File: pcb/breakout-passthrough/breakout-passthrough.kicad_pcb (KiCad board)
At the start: 4 copper layers, 38.4 x 62 mm, 2 parts, among them J1 FX18-120P-0.8SV20, J2 FX18-120S-0.8SV20

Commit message: [pass] ab based labels
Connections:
- net /IOB_102 renamed /HG_08
- net /IOB_56 renamed /LK_08
- net /IOB_57 renamed /LK_07
- net /IOB_61 renamed /LK_06
- net /IOB_63 renamed /LK_05
- net /IOB_64 renamed /LK_04
- net /IOB_71 renamed /LK_03
- net /IOB_72 renamed /LK_02
- net /IOB_73 renamed /LK_01
- net /IOB_79 renamed /JI_08
- net /IOB_80 renamed /JI_07
- net /IOB_81 renamed /JI_06
- net /IOB_82 renamed /JI_05
- net /IOB_91 renamed /JI_04
- net /IOB_94 renamed /JI_03
- net /IOB_95 renamed /JI_02
- net /IOB_96 renamed /JI_01
- net /IOL_10A renamed /GH_08
- net /IOL_10B renamed /IJ_01
- net /IOL_12A renamed /IJ_02
- net /IOL_12B renamed /IJ_03
- net /IOL_13A renamed /IJ_04
- net /IOL_13B renamed /IJ_05
- net /IOL_14B renamed /IJ_06
- net /IOL_17A renamed /IJ_07
- net /IOL_17B renamed /IJ_08
- net /IOL_18A renamed /KL_01
- net /IOL_18B renamed /KL_02
- net /IOL_23A renamed /KL_03
- net /IOL_23B renamed /KL_04
- net /IOL_24A renamed /KL_05
- net /IOL_24B renamed /KL_06
- net /IOL_25A renamed /KL_07
- net /IOL_25B renamed /KL_08
- net /IOL_4A renamed /GH_02
- net /IOL_4B renamed /GH_03
- net /IOL_5A renamed /GH_04
- net /IOL_5B renamed /GH_05
- net /IOL_8A renamed /GH_06
- net /IOL_8B renamed /GH_07
- net /IOR_109 renamed /HG_07
- net /IOR_110 renamed /HG_06
- net /IOR_111 renamed /HG_05
- net /IOR_112 renamed /HG_04
- net /IOR_114 renamed /HG_03
- net /IOR_115 renamed /HG_02
- net /IOR_116 renamed /HG_01
- net /IOR_117 renamed /FE_08
- net /IOR_118 renamed /FE_07
- net /IOR_119 renamed /FE_06
- net /IOR_120 renamed /FE_05
- net /IOR_128 renamed /FE_04
- net /IOR_136 renamed /FE_03
- net /IOR_137 renamed /FE_02
- net /IOR_138 renamed /FE_01
- net /IOR_139 renamed /DC_08
- net /IOR_140 renamed /DC_07
- net /IOR_141 renamed /DC_06
- net /IOR_144 renamed /DC_05
- net /IOR_146 renamed /DC_04
- net /IOR_147 renamed /DC_03
- net /IOR_148 renamed /DC_02
- net /IOR_152 renamed /DC_01
- net /IOR_160 renamed /BA_08
- net /IOR_161 renamed /BA_07
- net /IOR_164 renamed /BA_06
- net /IOR_165 renamed /BA_05
- net /IOR_166 renamed /BA_04
- net /IOR_167 renamed /BA_03
- net /IOT_168 renamed /BA_02
- net /IOT_169 renamed /BA_01
- net /IOT_170 renamed /CD_08
- net /IOT_171 renamed /CD_07
- net /IOT_172 renamed /CD_06
- net /IOT_173 renamed /CD_05
- net /IOT_174 renamed /CD_04
- net /IOT_177 renamed /CD_03
- net /IOT_178 renamed /CD_02
- net /IOT_179 renamed /CD_01
- net /IOT_181 renamed /AB_08
- net /IOT_190 renamed /AB_07
- net /IOT_191 renamed /AB_06
- net /IOT_192 renamed /AB_05
- net /IOT_197 renamed /AB_04
- net /IOT_198 renamed /AB_03
- net /IOT_206 renamed /AB_02
- net /IOT_212 renamed /AB_01
- net /IOT_213 renamed /EF_01
- net /IOT_214 renamed /EF_02
- net /IOT_215 renamed /EF_03
- net /IOT_216 renamed /EF_04
- net /IOT_217 renamed /EF_05
- net /IOT_219 renamed /EF_06
- net /IOT_220 renamed /EF_07
- net /IOT_221 renamed /EF_08
- net /IOT_222 renamed /GH_01

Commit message: [pcb] prep work for FX18-120P footprint fix
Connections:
- net /+3V3 renamed +3V3
- net /AB_01 renamed /A_01
- net /AB_02 renamed /A_05
- net /AB_03 renamed /A_02
- net /AB_04 renamed /A_06
- net /AB_05 renamed /A_03
- net /AB_06 renamed /A_07
- net /AB_07 renamed /A_04
- net /AB_08 renamed /A_08
- net /BA_01 renamed /E_01
- net /BA_02 renamed /E_05
- net /BA_03 renamed /E_02
- net /BA_04 renamed /E_06
- net /BA_05 renamed /E_03
- net /BA_06 renamed /E_07
- net /BA_07 renamed /E_04
- net /BA_08 renamed /E_08
- net /CD_01 renamed /B_01
- net /CD_02 renamed /B_05
- net /CD_03 renamed /B_02
- net /CD_04 renamed /B_06
- net /CD_05 renamed /B_03
- net /CD_06 renamed /B_07
- net /CD_07 renamed /B_04
- net /CD_08 renamed /B_08
- net /DC_01 renamed /F_01
- net /DC_02 renamed /F_05
- net /DC_03 renamed /F_02
- net /DC_04 renamed /F_06
- net /DC_05 renamed /F_03
- net /DC_06 renamed /F_07
- net /DC_07 renamed /F_04
- net /DC_08 renamed /F_08
- net /EF_01 renamed /C_01
- net /EF_02 renamed /C_05
- net /EF_03 renamed /C_02
- net /EF_04 renamed /C_06
- net /EF_05 renamed /C_03
- net /EF_06 renamed /C_07
- net /EF_07 renamed /C_04
- net /EF_08 renamed /C_08
- net /FE_01 renamed /L_08
- net /FE_02 renamed /L_04
- net /FE_03 renamed /L_07
- net /FE_04 renamed /L_03
- net /FE_05 renamed /L_06
- net /FE_06 renamed /L_02
- net /FE_07 renamed /L_05
- net /FE_08 renamed /L_01
- net /GH_01 renamed /D_01
- net /GH_02 renamed /D_05
- net /GH_03 renamed /D_02
- net /GH_04 renamed /D_06
- net /GH_05 renamed /D_03
- net /GH_06 renamed /D_07
- net /GH_07 renamed /D_04
- net /GH_08 renamed /D_08
- net /HG_01 renamed /I_01
- net /HG_02 renamed /I_05
- net /HG_03 renamed /I_02
- net /HG_04 renamed /I_06
- net /HG_05 renamed /I_03
- net /HG_06 renamed /I_07
- net /HG_07 renamed /I_04
- net /HG_08 renamed /I_08
- net /IJ_01 renamed /G_01
- net /IJ_02 renamed /G_05
- net /IJ_03 renamed /G_02
- net /IJ_04 renamed /G_06
- net /IJ_05 renamed /G_03
- net /IJ_06 renamed /G_07
- net /IJ_07 renamed /G_04
- net /IJ_08 renamed /G_08
- net /JI_01 renamed /K_08
- net /JI_02 renamed /K_04
- net /JI_03 renamed /K_07
- net /JI_04 renamed /K_03
- net /JI_05 renamed /K_06
- net /JI_06 renamed /K_02
- net /JI_07 renamed /K_05
- net /JI_08 renamed /K_01
- net /KL_01 renamed /H_01
- net /KL_02 renamed /H_05
- net /KL_03 renamed /H_02
- net /KL_04 renamed /H_06
- net /KL_05 renamed /H_03
- net /KL_06 renamed /H_07
- net /KL_07 renamed /H_04
- net /KL_08 renamed /H_08
- net /LK_01 renamed /J_01
- net /LK_02 renamed /J_05
- net /LK_03 renamed /J_02
- net /LK_04 renamed /J_06
- net /LK_05 renamed /J_03
- net /LK_06 renamed /J_07
- net /LK_07 renamed /J_04
- net /LK_08 renamed /J_08

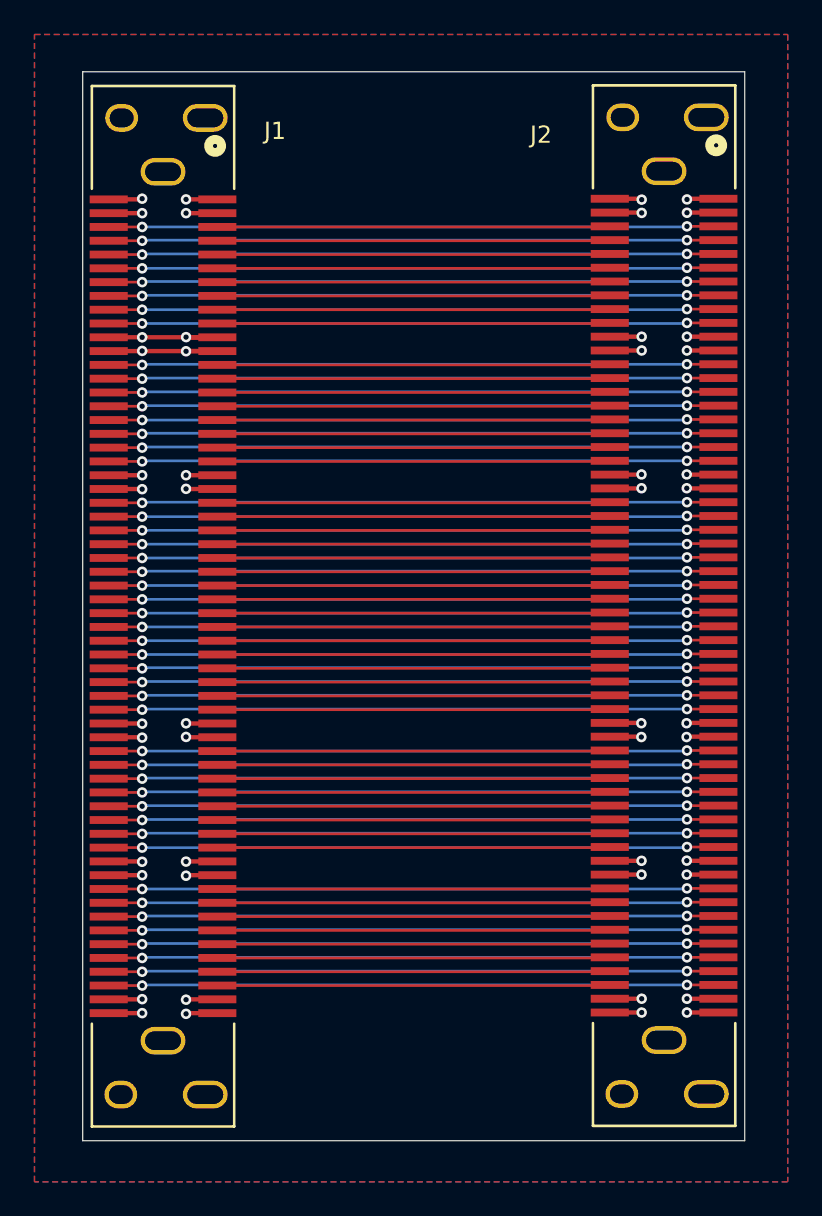
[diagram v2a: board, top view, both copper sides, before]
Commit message: [pcb] add FX18-120P footprint and update pcbs
and a few adc fixes, including a key resistor fix
(the op amp for Y had a copy paste error from X
on the positive Rg)
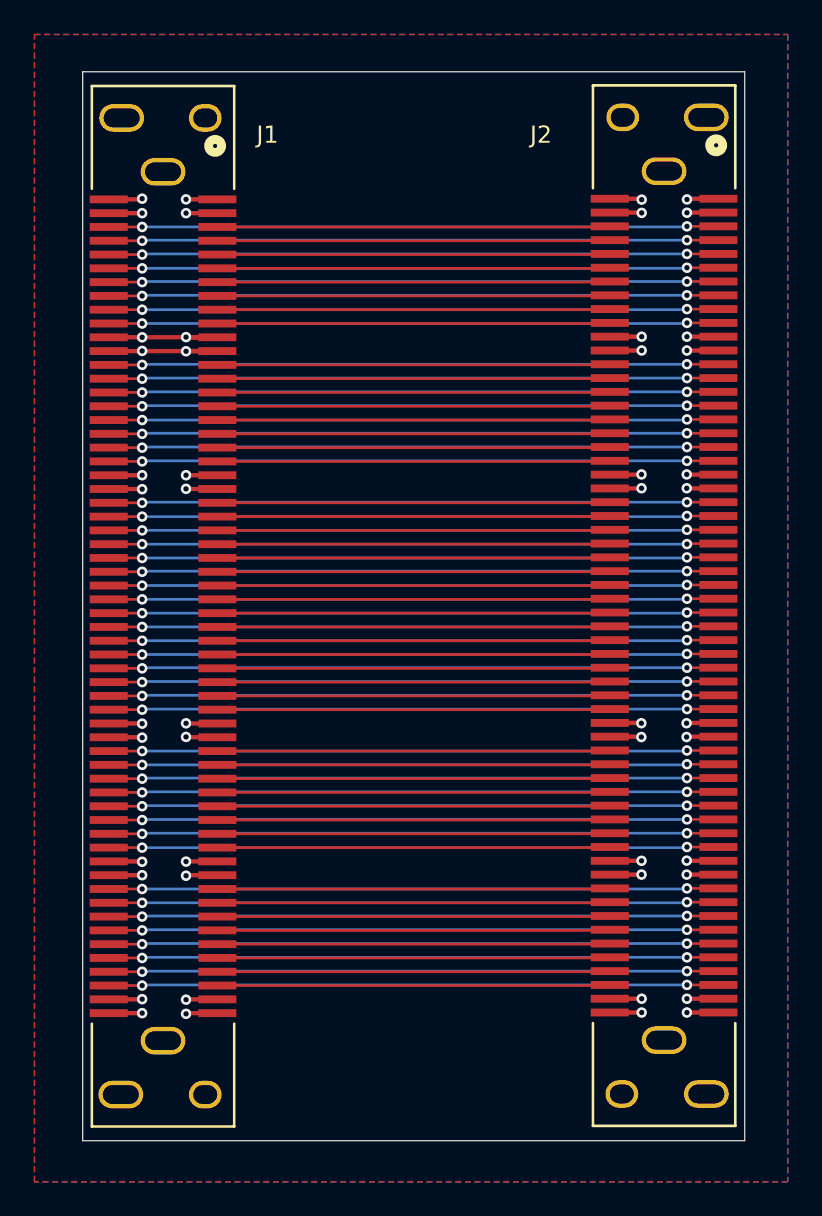
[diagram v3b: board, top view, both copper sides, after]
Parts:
- J1: footprint custom:CUSTOM_FX_120S-0.8SH20 -> custom:CUSTOM_FX_120P-0.8SH20
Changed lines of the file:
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@@
 		)
 	)
-	(footprint "custom:CUSTOM_FX_120S-0.8SH20"
+	(footprint "custom:CUSTOM_FX_120P-0.8SH20"
 		(layer "F.Cu")
 		(at 51.144 85.488 -90)
 		(tags "FX18-120S-0.8SV20 ")
 		(property "Reference" "J1"
-			(at -27.57 -6.489999 0)
+			(at -27.344997 -6.056 0)
 			(unlocked yes)
 			(layer "F.SilkS")
@@
 			)
 		)
-		(property "Footprint" "custom:CUSTOM_FX_120S-0.8SH20"
+		(property "Footprint" "custom:CUSTOM_FX_120P-0.8SH20"
 			(at 0 0 -90)
 			(unlocked yes)
@@
 		)
 		(pad "121" thru_hole oval
-			(at -28.325 2.4)
+			(at -28.325 -2.45)
 			(size 1.908 1.608)
 			(drill oval 1.4 1.1)
@@
 		)
 		(pad "122" thru_hole oval
-			(at -28.325 -2.45)
+			(at -28.325 2.4)
 			(size 2.608001 1.608)
 			(drill oval 2.1 1.1)
@@
 		)
 		(pad "125" thru_hole oval
-			(at 28.325 2.45)
+			(at 28.325 -2.45)
 			(size 1.908 1.608)
 			(drill oval 1.4 1.1)
@@
 		)
 		(pad "126" thru_hole oval
-			(at 28.325 -2.45)
+			(at 28.325 2.45)
 			(size 2.608001 1.608)
 			(drill oval 2.1 1.1)
